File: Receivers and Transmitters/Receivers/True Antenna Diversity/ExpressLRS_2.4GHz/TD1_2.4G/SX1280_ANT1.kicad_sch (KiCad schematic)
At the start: 8 parts, among them U2 SX1280IMLTRT, Y1 52MHz

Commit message: Updated schematics for TD1_2.4G receiver: ESP32, SX1280, and RFX2401C blocks
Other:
- company: https://github.com/Paschalis | TeodoraMiu -> https://github.com/Paschalis
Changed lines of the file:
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@@
 		(date "2025-02-23")
 		(rev "1.0")
-		(company "https://github.com/Paschalis | TeodoraMiu")
+		(company "https://github.com/Paschalis")
 		(comment 2 "capabilities in LoRa communication, making it ideal for reliable telemetry.")
 		(comment 3 "The SX1280 is used for its long-range, low-power, and high-performance ")

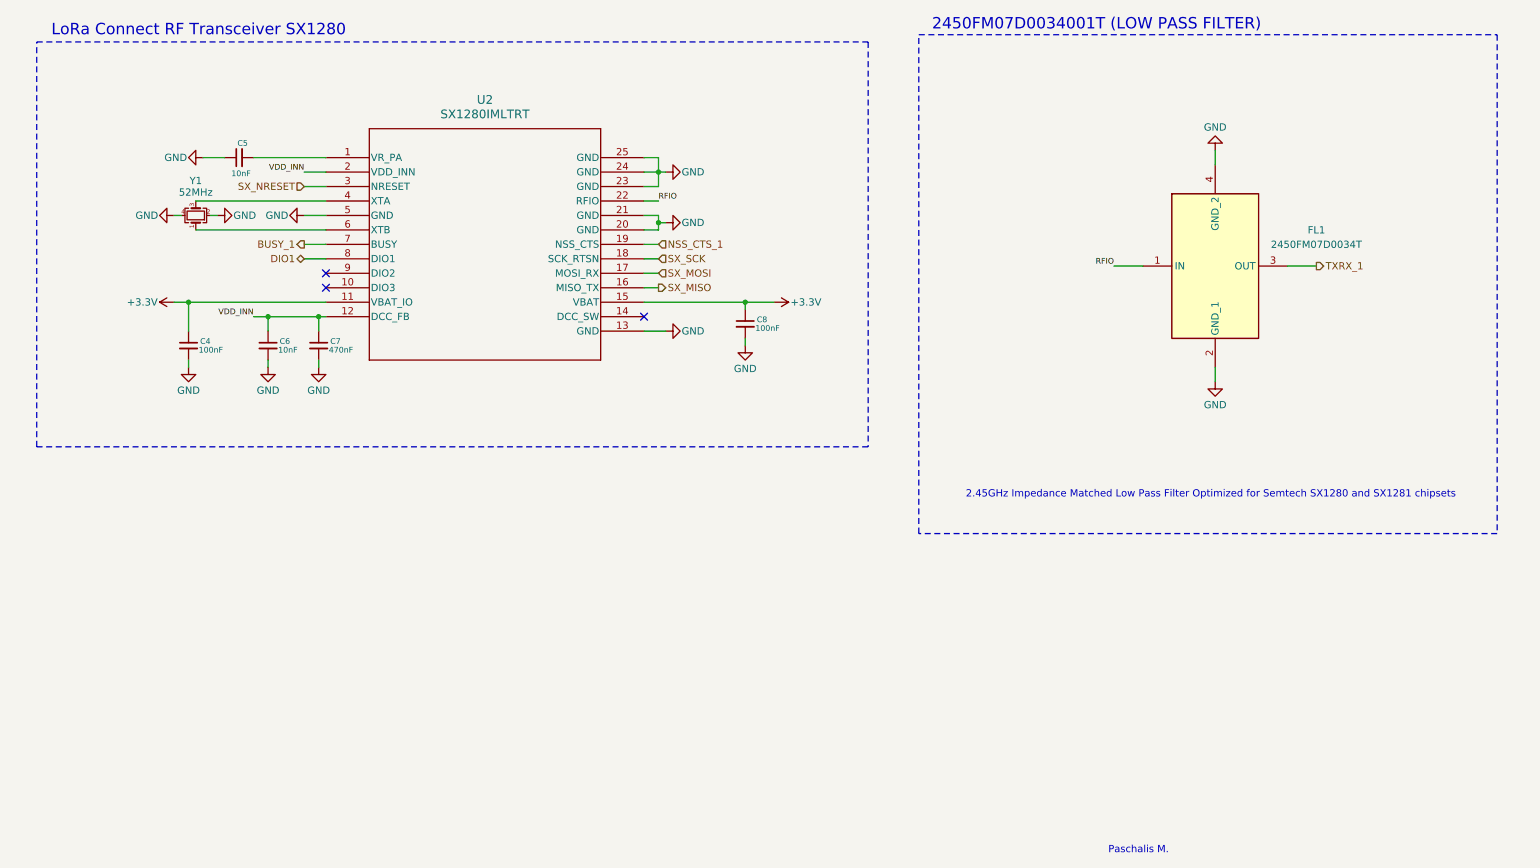
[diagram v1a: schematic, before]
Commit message: Update TD1_2.4G: schematic and PCB revisions, BOM export, README; remove old PCBWay production files
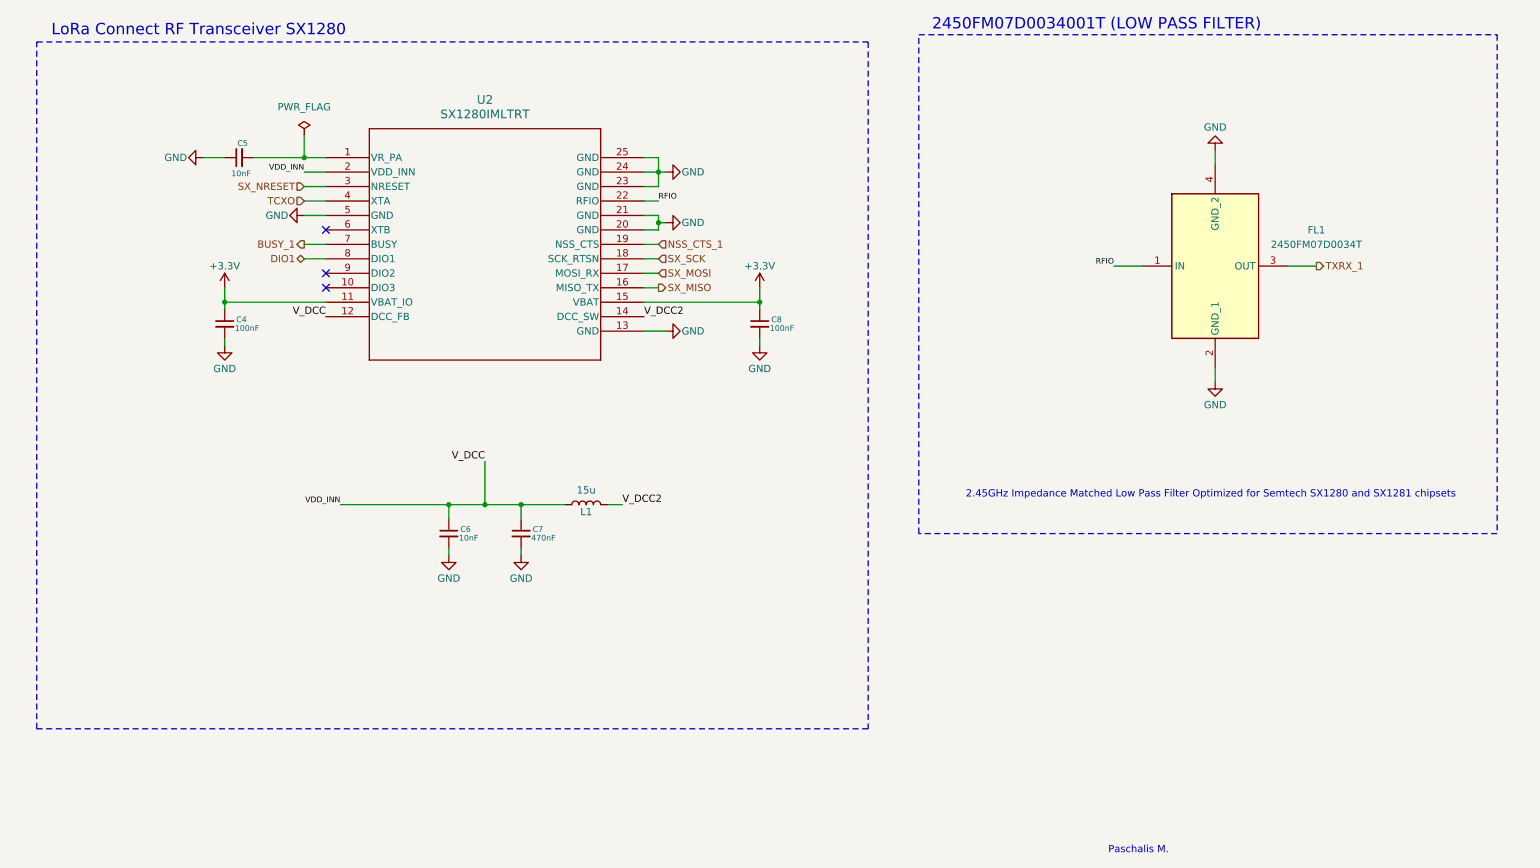
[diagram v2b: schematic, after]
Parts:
- removed Y1: 52MHz, Crystal:Crystal_SMD_2016-4Pin_2.0x1.6mm, symbol Device:Crystal_GND24_Small
- added L1: 15u, Inductor_SMD:L_0805_2012Metric, symbol Device:L
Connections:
- net VDD_INN: now also L1.1
- net V_DCC2: now reaches U2.14 (DCC_SW)
- net V_DCC2: now also L1.2
- net TCXO: now reaches U2.4 (XTA)
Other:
- moved on the sheet: C4, C6, C7, C8
